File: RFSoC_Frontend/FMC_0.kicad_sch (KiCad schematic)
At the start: 1 part, among them J9 LPAM-40-01.0-X-08-X-K-TR

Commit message: updated design for fixes
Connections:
- net ADCIO_05: no longer J9.B05
- new net ADCIO_04: J9.B05
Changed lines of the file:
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@@
     (effects (font (size 1.27 1.27)) (justify left bottom))
   )
-  (label "ADCIO_05" (at 193.04 355.6 0)
+  (label "ADCIO_04" (at 193.04 355.6 0)
     (effects (font (size 1.27 1.27)) (justify left bottom))
   )

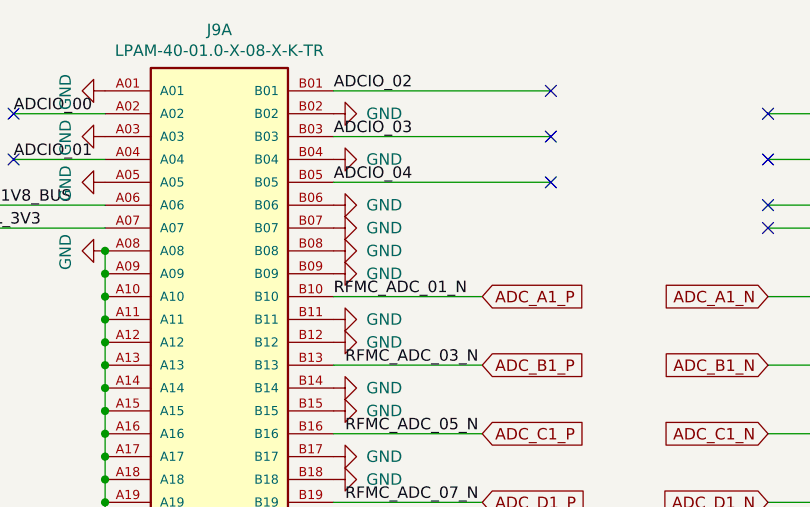
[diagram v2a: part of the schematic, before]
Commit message: fixed grounded util 3v3 pins on the LPAM Cnctr
updated to REV B
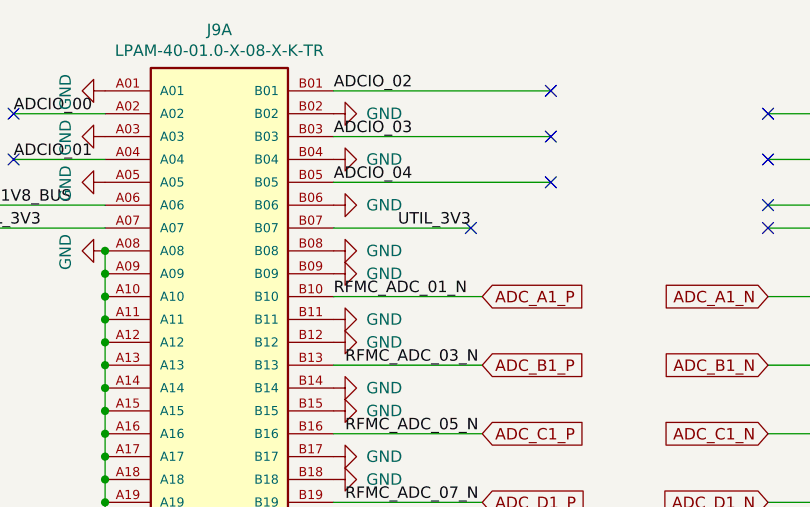
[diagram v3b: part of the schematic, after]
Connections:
- net GND: no longer J9.B07
- net UTIL_3V3: now also J9.B07
- no-connect marks 63 -> 64
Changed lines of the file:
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@@
   (no_connect (at 217.17 345.44))
   (no_connect (at 241.3 360.68))
+  (no_connect (at 208.28 360.68))
   (no_connect (at 420.37 431.8))
   (no_connect (at 330.2 360.68))
@@
     (stroke (width 0) (type default) (color 0 0 0 0))
   )
+  (wire (pts (xy 208.28 360.68) (xy 193.04 360.68))
+    (stroke (width 0) (type default) (color 0 0 0 0))
+  )
   (wire (pts (xy 347.98 424.18) (xy 347.98 426.72))
     (stroke (width 0) (type default) (color 0 0 0 0))
@@
   (label "ADC_CLKIN_0_P" (at 247.65 434.34 0)
     (effects (font (size 1.27 1.27)) (justify left bottom))
+  )
+  (label "UTIL_3V3" (at 208.28 360.68 180)
+    (effects (font (size 1.27 1.27)) (justify right bottom))
   )
   (label "UTIL_3V3" (at 375.92 360.68 0)
@@
       (effects (font (size 1.27 1.27)) hide)
     )
-    (pin "1")
-  )
-  (symbol (lib_id "power:GND") (at 193.04 360.68 90) (unit 1)
-    (in_bom yes) (on_board yes)
-    (property "Reference" "#PWR0225" (id 0) (at 199.39 360.68 0)
-      (effects (font (size 1.27 1.27)) hide)
-    )
-    (property "Value" "GND" (id 1) (at 200.66 360.68 90)
-      (effects (font (size 1.27 1.27)) (justify left))
-    )
-    (property "Footprint" "" (id 2) (at 193.04 360.68 0)
-      (effects (font (size 1.27 1.27)) hide)
-    )
-    (property "Datasheet" "" (id 3) (at 193.04 360.68 0)
-      (effects (font (size 1.27 1.27)) hide)
-    )
